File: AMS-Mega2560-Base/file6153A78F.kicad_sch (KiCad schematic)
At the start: 21 parts, among them IC7 LTV-846S, Q1 2N7000, Q2 2N7000, Q3 2N7000, Q4 2N7000

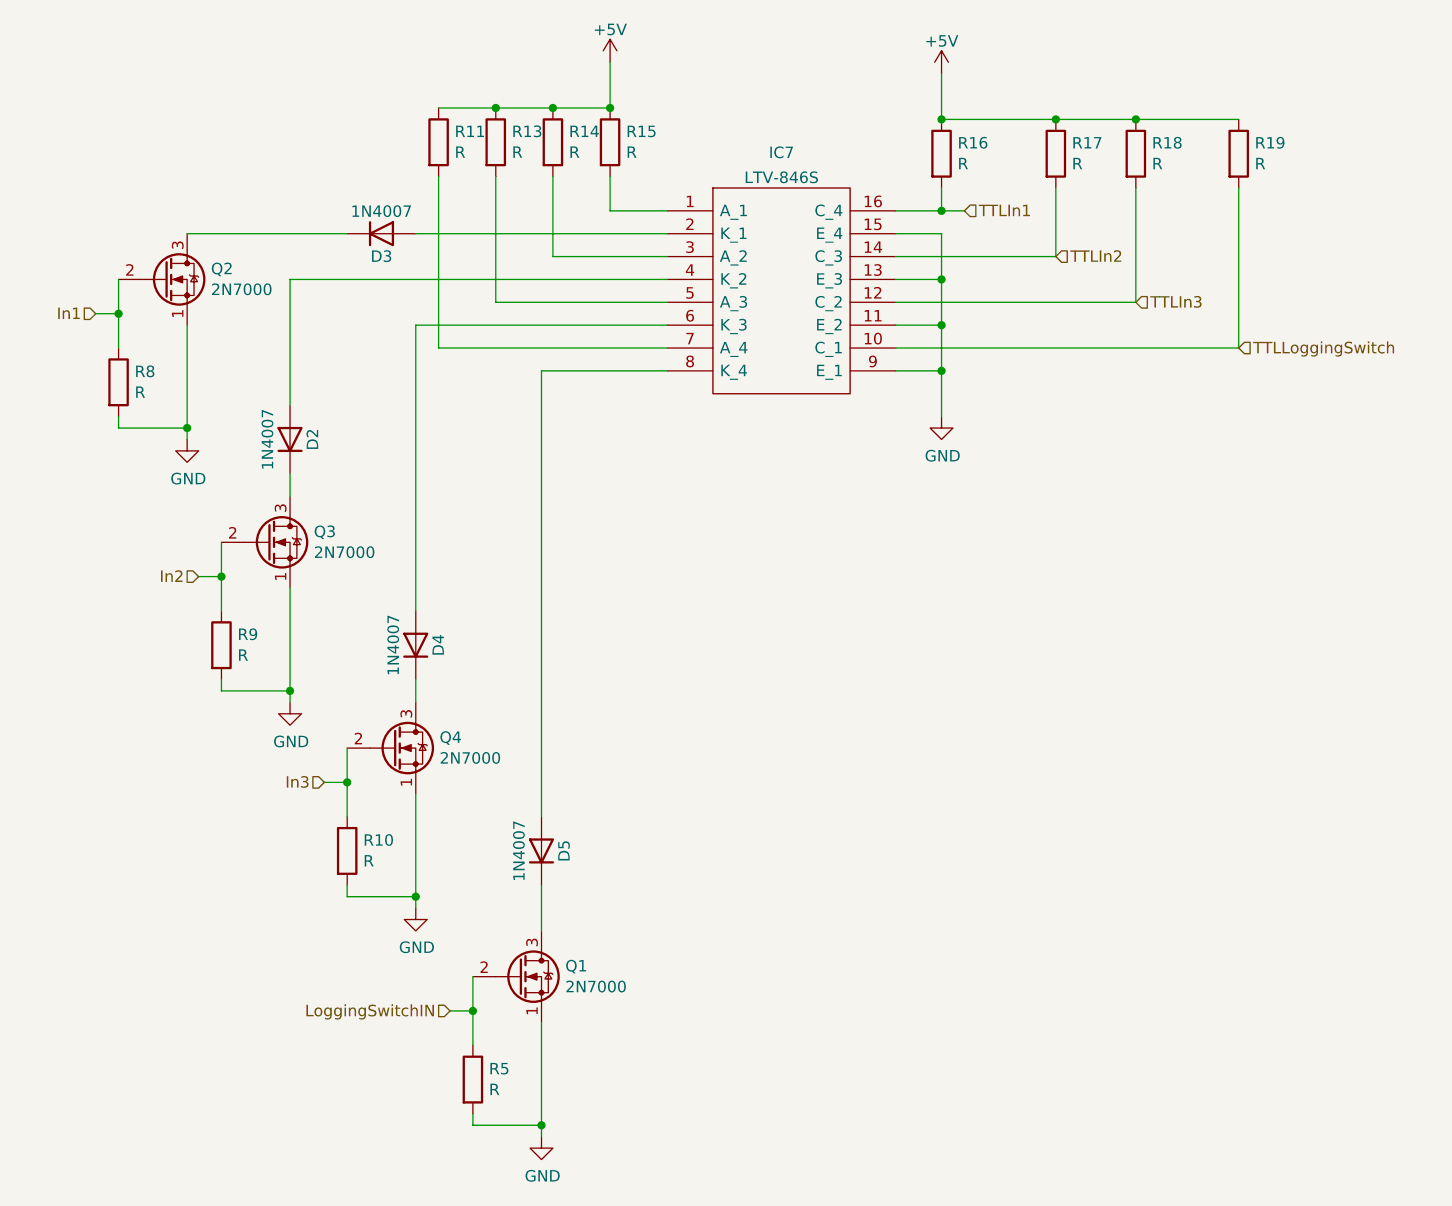
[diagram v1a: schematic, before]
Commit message: applying some fixes for the RPM sensor and other parts of the schem
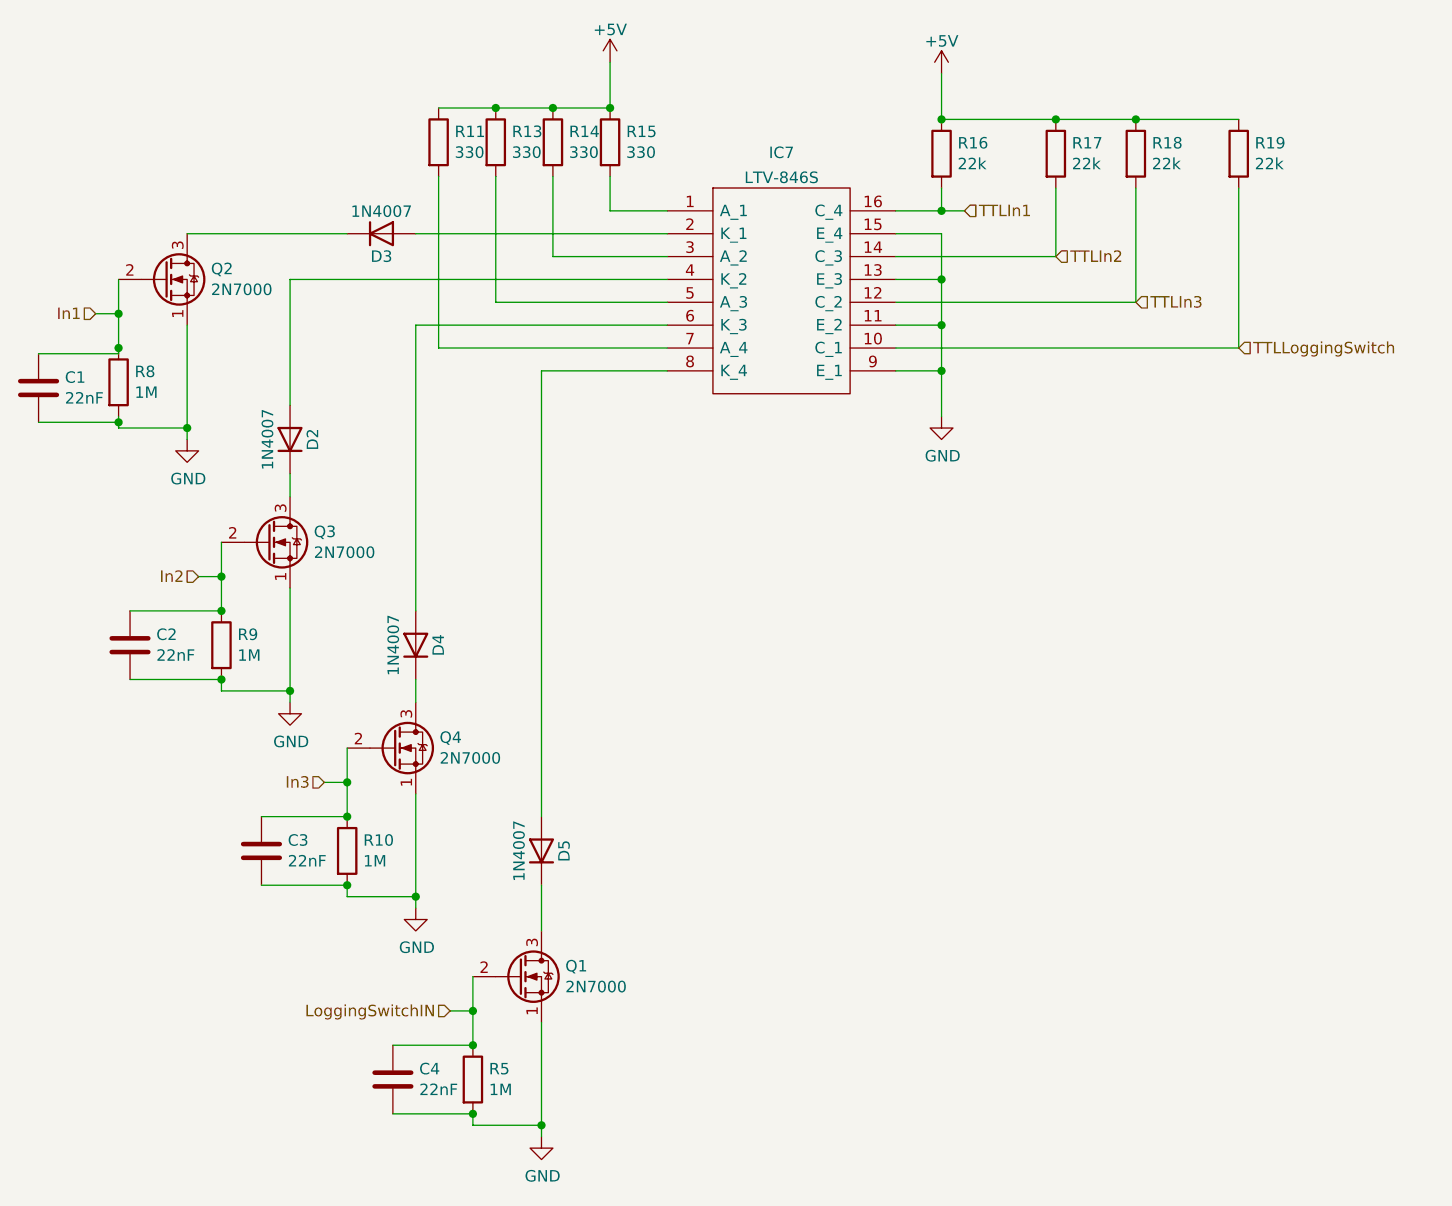
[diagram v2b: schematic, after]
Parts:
- added C1, C2, C3, C4: 22nF, Capacitor_THT:C_Disc_D4.7mm_W2.5mm_P5.00mm, symbol Device:C
- R10, R5, R8, R9: value R -> 1M
- R11, R13, R14, R15: value R -> 330
- R16, R17, R18, R19: value R -> 22k
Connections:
- net GND: now also C1.2, C2.2, C3.2, C4.2
- net In1: now also C1.1
- net In2: now also C2.1
- net In3: now also C3.1
- net LoggingSwitchIN: now also C4.1

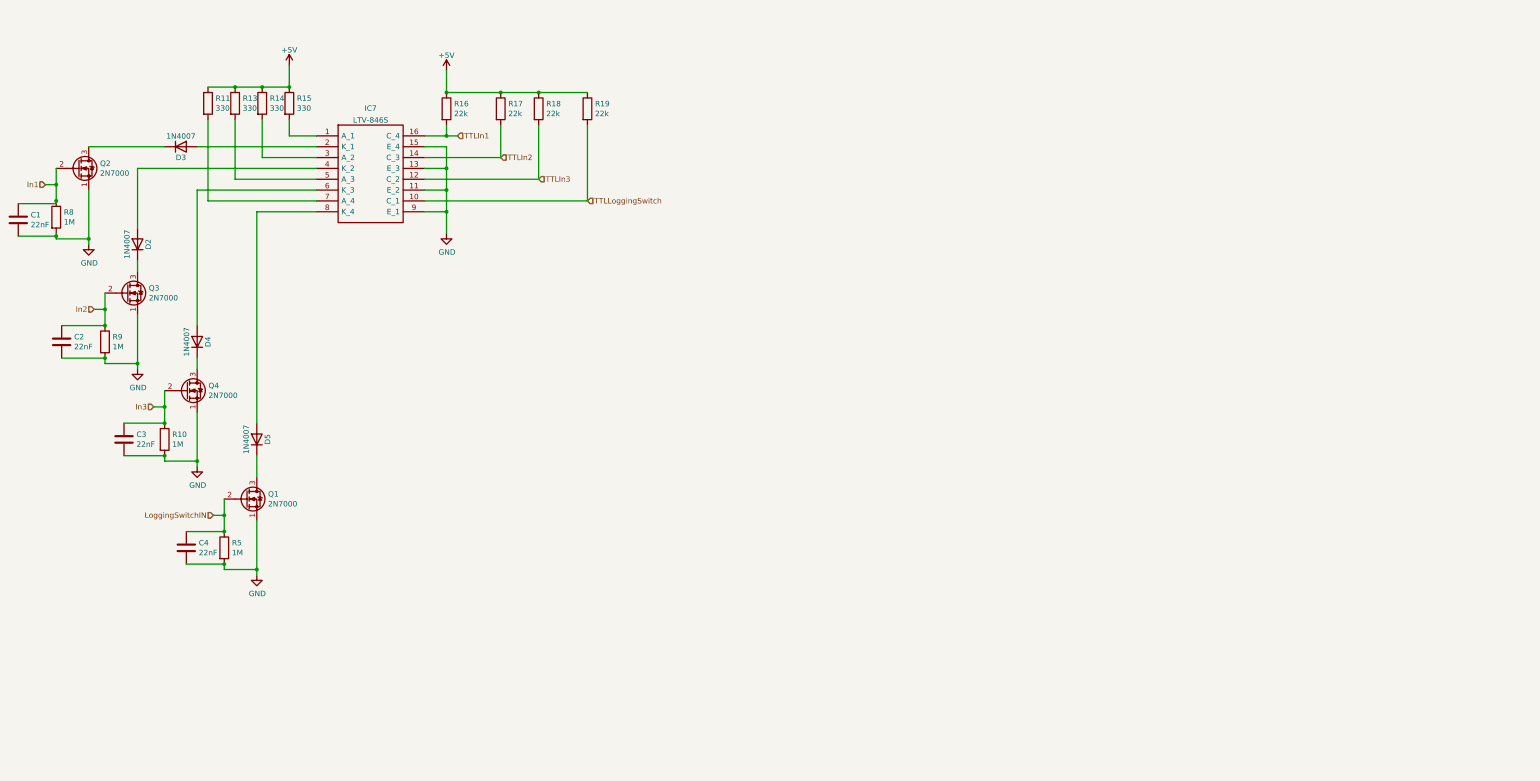
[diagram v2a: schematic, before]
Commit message: updating the inputs and reannotating some stuff.
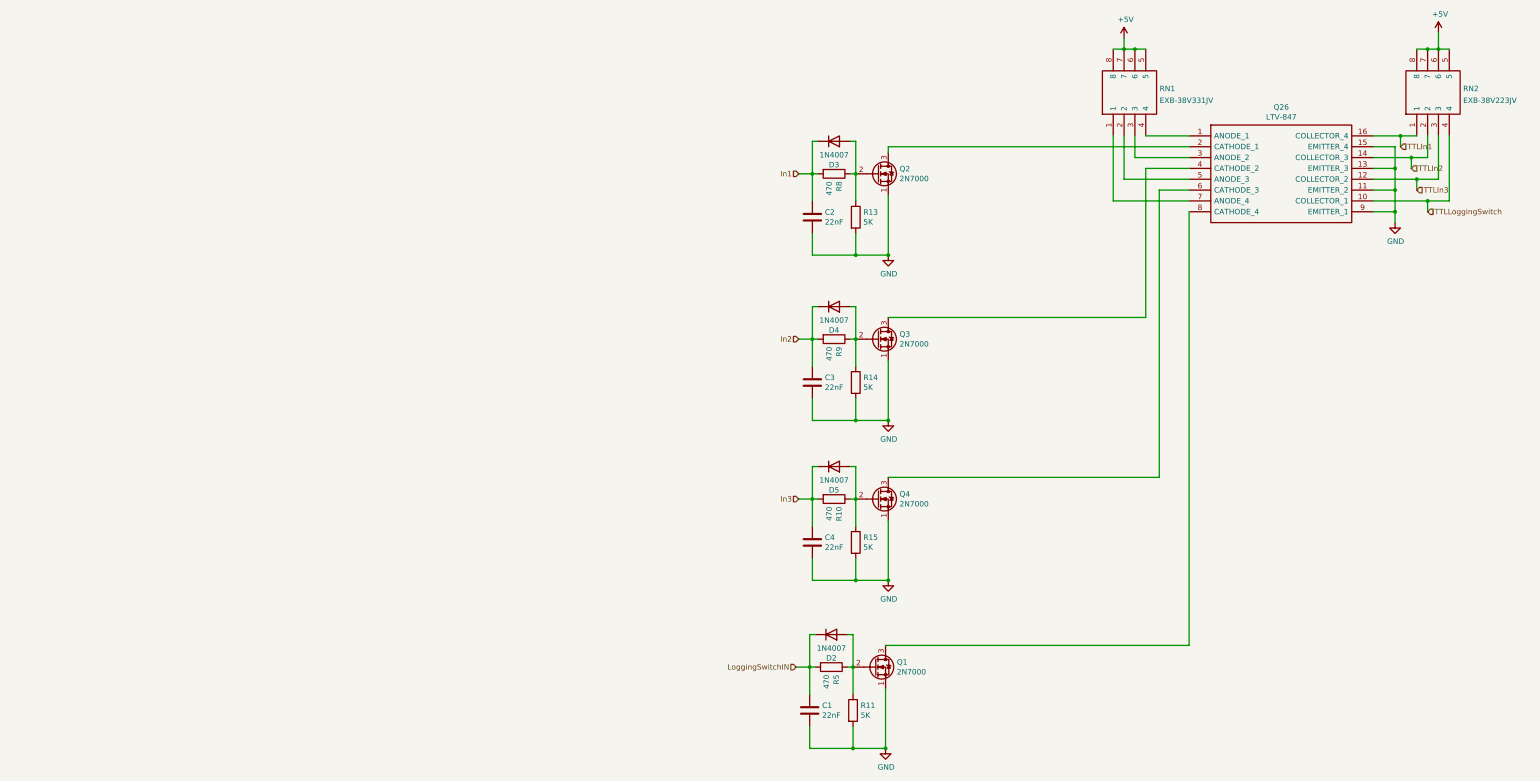
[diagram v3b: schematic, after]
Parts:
- removed IC7: LTV-846S, SamacSys_Parts:SOP254P1016X460-16N, symbol Samac_Sys:LTV-846S
- removed R16, R17, R18, R19: 22k, Resistor_THT:R_Axial_DIN0207_L6.3mm_D2.5mm_P2.54mm_Vertical, symbol Device:R
- added Q26: LTV-847, SamacSys_Parts:DIP762W60P254L1984H450Q16N, symbol SamacSys_Parts:LTV-847
- added RN1: EXB-38V331JV, EXB38V472JV, symbol Samac_Sys:EXB-38V331JV
- added RN2: EXB-38V223JV, EXB38V472JV, symbol Samac_Sys:EXB-38V223JV
- C1, C2, C3, C4: footprint Capacitor_THT:C_Disc_D4.7mm_W2.5mm_P5.00mm -> Capacitor_SMD:C_0603_1608Metric_Pad1.08x0.95mm_HandSolder
- R10, R5, R8, R9: value 1M -> 470
- R11, R13, R14, R15: value 330 -> 5K
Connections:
- net +5V: now also RN1.5, RN1.6, RN1.7, RN1.8, RN2.5, RN2.6, RN2.7, RN2.8; no longer R11.1, R13.1, R14.1, R15.1
- net GND: now also R11.2, R13.2, R14.2, R15.2, Q26.11 (EMITTER_2), Q26.13 (EMITTER_3), Q26.15 (EMITTER_4), Q26.9 (EMITTER_1); no longer R10.2, R5.2, R8.2, R9.2
- net In1: now also C2.1, D3.1 (K), R8.2; no longer C1.1, Q2.2 (G), R8.1
- net In2: now also C3.1, D4.1 (K), R9.2; no longer C2.1, Q3.2 (G), R9.1
- net In3: now also C4.1, D5.1 (K), R10.2; no longer C3.1, Q4.2 (G), R10.1
- net LoggingSwitchIN: now also C1.1, D2.1 (K), R5.2; no longer C4.1, Q1.2 (G), R5.1
- net TTLIn1: now also Q26.16 (COLLECTOR_4), RN2.1
- net TTLIn2: now also Q26.14 (COLLECTOR_3), RN2.2
- net TTLIn3: now also Q26.12 (COLLECTOR_2), RN2.3
- net TTLLoggingSwitch: now also Q26.10 (COLLECTOR_1), RN2.4
- net at Q3.3 (D): now also Q26.4 (CATHODE_2); no longer D2.1 (K)
- net at Q2.3 (D): now also Q26.2 (CATHODE_1); no longer D3.1 (K)
- net at D3.2 (A): now also Q2.2 (G), R13.1, R8.1
- net at Q1.3 (D): now also Q26.8 (CATHODE_4); no longer D5.1 (K)
- net at D5.2 (A): now also Q4.2 (G), R10.1, R15.1
- net at D2.2 (A): now also Q1.2 (G), R11.1, R5.1
- net at Q4.3 (D): now also Q26.6 (CATHODE_3); no longer D4.1 (K)
- net at D4.2 (A): now also Q3.2 (G), R14.1, R9.1
- new net: Q26.7 (ANODE_4), RN1.1
- new net: Q26.5 (ANODE_3), RN1.2
- new net: Q26.3 (ANODE_2), RN1.3
- new net: Q26.1 (ANODE_1), RN1.4

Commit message: working on this.
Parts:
- added C5, C6, C7, C8: 22nF, Capacitor_SMD:C_0603_1608Metric_Pad1.08x0.95mm_HandSolder, symbol Device:C
- added D1, D6, D7, D8: 1N4007, Diode_THT:D_DO-41_SOD81_P10.16mm_Horizontal, symbol Diode:1N4007
- added Q21: LTV-847, SamacSys_Parts:DIP762W60P254L1984H450Q16N, symbol SamacSys_Parts:LTV-847
- added Q23, Q24, Q25, Q27: 2N7000, Package_TO_SOT_THT:TO-92_Inline, symbol Transistor_FET:2N7000
- added R30, R31, R32, R33: 470, Resistor_THT:R_Axial_DIN0207_L6.3mm_D2.5mm_P2.54mm_Vertical, symbol Device:R
- added R34, R35, R36, R37: 5K, Resistor_THT:R_Axial_DIN0207_L6.3mm_D2.5mm_P2.54mm_Vertical, symbol Device:R
- added R38, R60, R61, R62: 330, Resistor_THT:R_Axial_DIN0207_L6.3mm_D2.5mm_P2.54mm_Vertical, symbol Device:R
- added RN3: EXB-38V223JV, EXB38V472JV, symbol Samac_Sys:EXB-38V223JV
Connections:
- net +5V: now also Q21.1 (ANODE_1), Q21.10 (COLLECTOR_1), Q21.12 (COLLECTOR_2), Q21.14 (COLLECTOR_3), Q21.16 (COLLECTOR_4), Q21.3 (ANODE_2), Q21.5 (ANODE_3), Q21.7 (ANODE_4)
- net GND: now also C5.2, C6.2, C7.2, C8.2, R34.2, R35.2, R36.2, R37.2, R38.2, R60.2, R61.2, R62.2, RN3.1, RN3.2, RN3.3, RN3.4
- net In1: now also C6.1, D6.1 (K), R31.2
- net In2: now also C7.1, D7.1 (K), R32.2
- net In3: now also C8.1, D8.1 (K), R33.2
- net LoggingSwitchIN: now also C5.1, D1.1 (K), R30.2
- net TTLIn1: now also Q21.15 (EMITTER_4), RN3.8
- net TTLIn2: now also Q21.13 (EMITTER_3), RN3.7
- net TTLIn3: now also Q21.11 (EMITTER_2), RN3.6
- net TTLLoggingSwitch: now also Q21.9 (EMITTER_1), RN3.5
- new net: D1.2 (A), Q23.2 (G), R30.1, R34.1
- new net: Q21.2 (CATHODE_1), Q24.3 (D)
- new net: Q21.4 (CATHODE_2), Q25.3 (D)
- new net: Q21.6 (CATHODE_3), Q27.3 (D)
- new net: Q21.8 (CATHODE_4), Q23.3 (D)
- new net: D7.2 (A), Q25.2 (G), R32.1, R36.1
- new net: Q25.1 (S), R60.1
- new net: Q27.1 (S), R61.1
- new net: D6.2 (A), Q24.2 (G), R31.1, R35.1
- new net: D8.2 (A), Q27.2 (G), R33.1, R37.1
- new net: Q23.1 (S), R62.1
- new net: Q24.1 (S), R38.1
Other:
- moved on the sheet: C1, C2, C3, C4, D2, D3, D4, D5, Q1, Q2, Q26, Q3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

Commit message: * Schematic ** finished CAN bus Design work ** updated the input circuits to my standard design and removed the old one that was funky
* PCB
** updated footprints
** removed the old parts/designed
** starting prep for placing parts
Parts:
- removed C1, C2, C3, C4, C5, C6, C7, C8: 22nF, Capacitor_SMD:C_0603_1608Metric_Pad1.08x0.95mm_HandSolder, symbol Device:C
- removed D1, D2, D3, D4, D5, D6, D7, D8: 1N4007, Diode_THT:D_DO-41_SOD81_P10.16mm_Horizontal, symbol Diode:1N4007
- removed Q1, Q2, Q23, Q24, Q25, Q27, Q3, Q4: 2N7000, Package_TO_SOT_THT:TO-92_Inline, symbol Transistor_FET:2N7000
- removed Q26: LTV-847, SamacSys_Parts:DIP762W60P254L1984H450Q16N, symbol SamacSys_Parts:LTV-847
- removed R10, R30, R31, R32, R33, R5, R8, R9: 470, Resistor_THT:R_Axial_DIN0207_L6.3mm_D2.5mm_P2.54mm_Vertical, symbol Device:R
- removed R11, R13, R14, R15, R34, R35, R36, R37: 5K, Resistor_THT:R_Axial_DIN0207_L6.3mm_D2.5mm_P2.54mm_Vertical, symbol Device:R
- removed R38, R60, R61, R62: 330, Resistor_THT:R_Axial_DIN0207_L6.3mm_D2.5mm_P2.54mm_Vertical, symbol Device:R
- removed RN1: EXB-38V331JV, EXB38V472JV, symbol Samac_Sys:EXB-38V331JV
- removed RN2: EXB-38V223JV, EXB38V472JV, symbol Samac_Sys:EXB-38V223JV
- added C2 (x4): 220nF, Capacitor_THT:C_Disc_D5.1mm_W3.2mm_P5.00mm, symbol Device:C
- added Q17 (x4): BS250, Package_TO_SOT_THT:TO-92_Inline, symbol Transistor_FET:BS250
- added R41 (x4): 330, Resistor_THT:R_Axial_DIN0207_L6.3mm_D2.5mm_P2.54mm_Vertical, symbol Device:R
- added R42 (x4): 1K, Resistor_THT:R_Axial_DIN0207_L6.3mm_D2.5mm_P2.54mm_Vertical, symbol Device:R
- RN3: footprint EXB38V472JV -> SamacSys_Parts:EXB38V472JV
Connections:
- net GND: now also C2.2, C2.2, C2.2, C2.2, R41.2, R41.2, R41.2, R41.2
- net In1: now also C2.1, Q17.3 (S)
- net In2: now also C2.1, Q17.3 (S)
- net In3: now also C2.1, Q17.3 (S)
- net LoggingSwitchIN: now also C2.1, Q17.3 (S)
- net at Q21.2 (CATHODE_1): now also R42.2
- net at Q21.4 (CATHODE_2): now also R42.2
- net at Q21.6 (CATHODE_3): now also R42.2
- net at Q21.8 (CATHODE_4): now also R42.2
- new net: Q17.2 (G), R41.1 (x4)
- new net: Q17.1 (D), R42.1 (x4)
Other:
- moved on the sheet: Q21, RN3
